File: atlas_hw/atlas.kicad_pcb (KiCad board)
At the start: 4 copper layers, 71 x 73.4 mm, 192 parts, among them J1 USB_C_Receptacle_USB2.0, J10 PSP_LCD, J2 DEBUG_STM, J3 PSP_TOUCH, J4 DEBUG_NRF, J5 CELL_THERM, J8 Micro_SD_Card_Det, J9 PSP_LCD_BL, Q1 Q_NMOS_DGS, Q2 Q_NMOS_DGS, Q3 Q_NMOS_DGS, Q4 Q_NMOS_DGS, Q5 Q_NMOS_DGS, SW1 SReset, SW2 Power, SW3 ResetSTM, SW4 ResetNRF, U1 STM32H723VITx, U10 BQ25611D, U11 STM6601CA2BDM6F, U12 BGU7007, U13 LSF0108, U14 NPP600SNADJ, U15 TPS61073, U16 PAM2841, U2 W957A8MFYA5I, U3 MCP1811B, U4 TLV62569DBV, U5 nRF52810-QCxx, U6 LC709203F, U7 Teseo-LIV3F, U8 MS5637, U9 MC6470, Y1 16M, Y2 32k, Y3 32M, Y4 32k

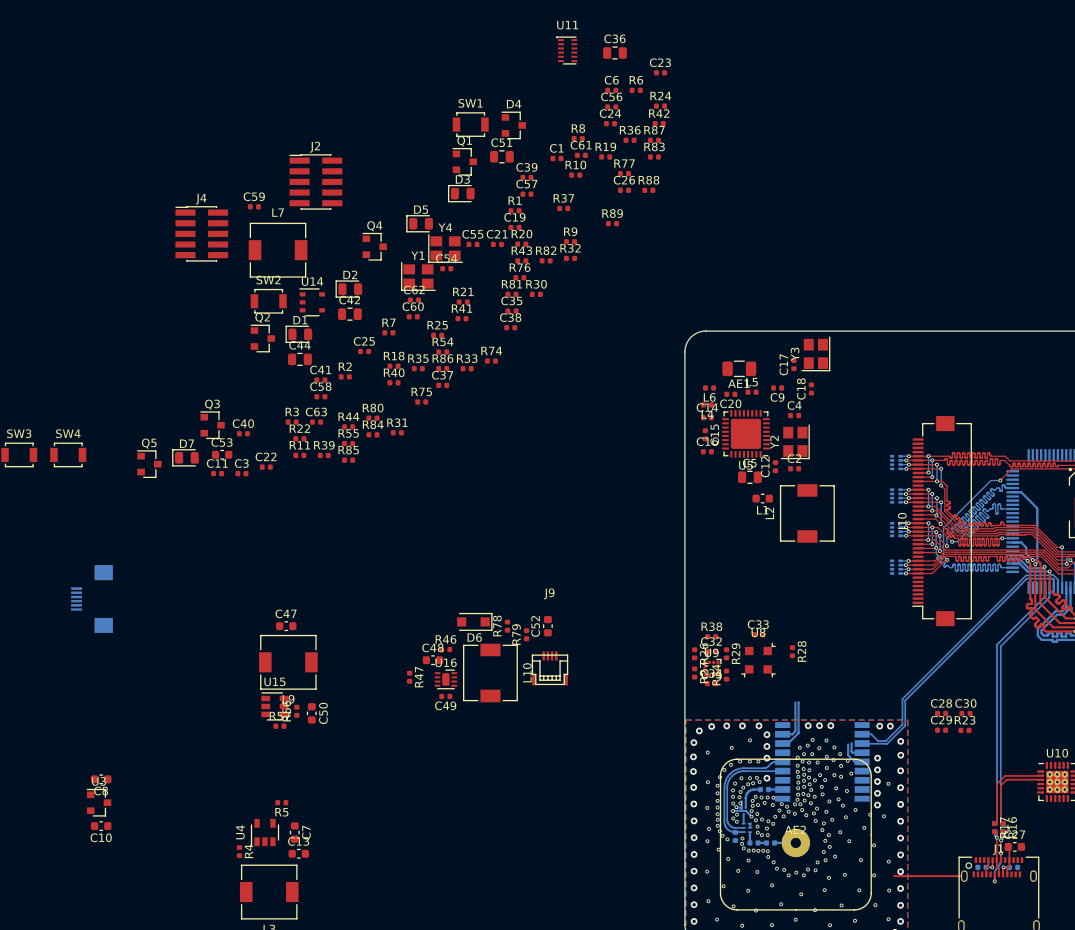
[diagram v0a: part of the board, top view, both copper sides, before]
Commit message: added attiny402 as sps
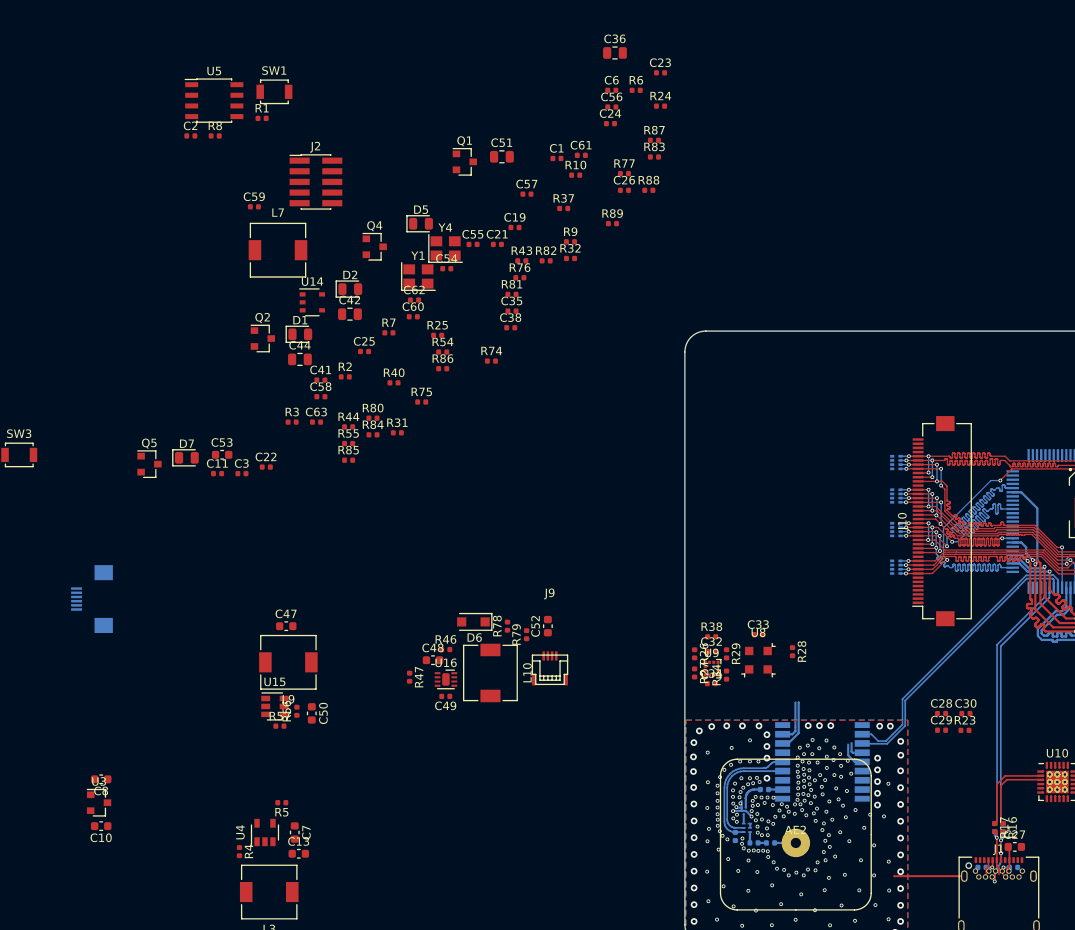
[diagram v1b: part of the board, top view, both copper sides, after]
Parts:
- removed AE1: CHIP, Resistor_SMD:R_1206_3216Metric
- removed C12: 100p, Capacitor_SMD:C_0402_1005Metric
- removed C14, C17, C18: 1p, Capacitor_SMD:C_0402_1005Metric
- removed C15: NP, Capacitor_SMD:C_0402_1005Metric
- removed C16, C39, C9: 0.1u, Capacitor_SMD:C_0402_1005Metric
- removed C20: 2.2p, Capacitor_SMD:C_0402_1005Metric
- removed C37, C40: 10u, Capacitor_SMD:C_0402_1005Metric
- removed C4: 12p, Capacitor_SMD:C_0402_1005Metric
- removed C5: 10u, Capacitor_SMD:C_0805_2012Metric
- removed D3: NRF_STATUS, LED_SMD:LED_0805_2012Metric
- removed D4: DC, Package_TO_SOT_SMD:SOT-23
- removed J4: DEBUG_NRF, Connector_PinHeader_1.27mm:PinHeader_2x05_P1.27mm_Vertical_SMD
- removed L1: 3.9n, Inductor_SMD:L_0603_1608Metric
- removed L2: 15u, Inductor_SMD:L_6.3x6.3_H3
- removed L4, L6: 3.9n, Inductor_SMD:L_0402_1005Metric
- removed L5: NP, Inductor_SMD:L_0402_1005Metric
- removed Q3: Q_NMOS_DGS, Package_TO_SOT_SMD:SOT-23
- removed R11, R35: 1k, Resistor_SMD:R_0402_1005Metric
- removed R18, R20, R21, R22, R41, R42: NP, Resistor_SMD:R_0402_1005Metric
- removed R19: 0, Resistor_SMD:R_0402_1005Metric
- removed R30: 10k, Resistor_SMD:R_0402_1005Metric
- removed R33, R36, R39: 100k, Resistor_SMD:R_0402_1005Metric
- removed SW2: Power, Button_Switch_SMD:SW_SPST_B3U-1000P
- removed SW4: ResetNRF, Button_Switch_SMD:SW_SPST_B3U-1000P
- removed U11: STM6601CA2BDM6F, Package_DFN_QFN:TDFN-12_2x3mm_P0.5mm
- removed Y2: 32k, Crystal:Crystal_SMD_3225-4Pin_3.2x2.5mm
- removed Y3: 32M, Crystal:Crystal_SMD_3225-4Pin_3.2x2.5mm
- C2: value 12p -> 0.1u
- J1: footprint Connector_USB:USB_C_Receptacle_Amphenol_12401610E4-2A -> Connector_USB:USB_C_Receptacle_Amphenol_12401548E4-2A
- R1: value 0 -> 100k
- SW1: value SReset -> ON_OFF
- U5: value nRF52810-QCxx -> ATtiny402-SS; footprint Package_DFN_QFN:QFN-32-1EP_5x5mm_P0.5mm_EP3.6x3.6mm -> Package_SO:SOIC-8_3.9x4.9mm_P1.27mm
- moved C2 82.3 mm to (134.4, 83.7)
- moved U5 74.9 mm to (137.2, 79.5), turned to 0 degrees
- moved R8 43.4 mm to (137.3, 83.7)
- moved R1 32.2 mm to (142.9, 81.6)
- moved SW1 23.8 mm to (144.4, 78.4)
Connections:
- net /BTN_DOWN renamed Net-(U1-Pad17)
- net /BTN_ENTER renamed Net-(U1-Pad16)
- net /BTN_LEFT renamed Net-(U1-Pad18)
- net /BTN_RIGHT renamed Net-(U1-Pad25)
- net /BTN_UP renamed Net-(U1-Pad24)
- net /EN_SD_PWR renamed Net-(U1-Pad85)
- net Net-(U5-Pad6) renamed /PWR_CTRL_UPDI
- C2 pad 2: /XL1_NRF -> /VCC_BACKUP
- C6 pad 1: Net-(C6-Pad1) -> /VCC_BACKUP
- R1 pad 1: Net-(C6-Pad1) -> /PWR_EN_O
- R8 pad 1: /NRF_STATUS -> /PWR_SW_I
- R8 pad 2: GND -> /VCC_BACKUP
- SW1 pad 2: Net-(R18-Pad1) -> /PWR_SW_I
- U1 pad 1: /SP4_SCK_NRF -> Net-(U1-Pad1)
- U1 pad 2: /NRF_INT -> Net-(U1-Pad2)
- U1 pad 4: /SP4_MISO_NRF -> Net-(U1-Pad4)
- U1 pad 5: /SP4_MOSI_NRF -> Net-(U1-Pad5)
- U1 pad 6: Net-(C6-Pad1) -> /VCC_BACKUP
- U1 pad 86: /PWR_MCU_HOLD -> /PWR_ACK_I
- U1 pad 87: /PWR_BTN_OUT -> /PWR_SW_O
- U1 pad 88: /PWR_MCU_INT -> Net-(U1-Pad88)
- U1 pad 97: /UART8_RX_NRF -> Net-(U1-Pad97)
- U1 pad 98: /UART8_TX_NRF -> Net-(U1-Pad98)
- U4 pad 1: /EN_MCU_PWR -> /PWR_EN_O
- U5 pad 1: /DEC1 -> /VCC_BACKUP
- U5 pad 2: /XL1_NRF -> /PWR_SW_I
- U5 pad 3: /XL2_NRF -> /PWR_EN_O
- U5 pad 4: Net-(U5-Pad4) -> /PWR_ACK_I
- U5 pad 5: Net-(U5-Pad5) -> /PWR_SW_O
- U5 pad 7: Net-(U5-Pad7) -> /DEBUG_NRESET_STM
- U5 pad 8: /NRF_INT -> GND
- U6 pad : GND -> (no net)
- U7 pad 10: GND -> Net-(C43-Pad2)
- U7 pad 11: Net-(C43-Pad2) -> (no net)
- U7 pad 18: Net-(U7-Pad18) -> (no net)

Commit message: rough blender model of casing further hw changes
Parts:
- removed AE2: 2088900001, atlas:2088900001
- removed C43, C46: 120p, Capacitor_SMD:C_0402_1005Metric
- removed C45: 0.1u, Capacitor_SMD:C_0402_1005Metric
- removed F1: B39162B8813P810, Filter:Filter_1109-5_1.1x0.9mm
- removed L8: 5n6, Inductor_SMD:L_0402_1005Metric
- removed U12: BGU7007, atlas:6-XSON_1.5x1.0mm_0.5mm
- removed U7: Teseo-LIV3F, RF_Module:ublox_MAX
- added REF**: BGM220P, atlas:BGM220P, F.Cu at (229.8, 83.3)
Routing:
- net /GPS_VCC_RF: track 15.7 -> 0.00 mm
- net /GPS_ANT_OFF: track 14.2 -> 0.00 mm
- net /LPUART1_RX_GPS: track 34.5 -> 24.8 mm
- net /LPUART1_TX_GPS: track 34.9 -> 25.9 mm
- net /I2C_SDA_SENSOR: track 6.08 -> 0.00 mm
- net /I2C_SCL_SENSOR: track 5.11 -> 0.00 mm
- net GND: track 13.2 -> 8.39 mm, vias 253 -> 0
- net Net-(C43-Pad1): track 3.54 -> 0.00 mm
- net /GPS_WAKEUP: track 3.29 -> 0.00 mm
- net Net-(AE2-Pad1): track 2.86 -> 0.00 mm
- net /GPS_1PPS: track 2.35 -> 0.00 mm
- net Net-(C43-Pad2): track 1.69 -> 0.00 mm
- net Net-(L8-Pad1): track 1.24 -> 0.00 mm
- net Net-(F1-Pad1): track 1.06 -> 0.00 mm
- net Net-(C46-Pad2): track 1.00 -> 0.00 mm
- removed copper zone on B.Cu, net GND
- removed copper zone on F.Cu, net GND
- removed copper zone on In1.Cu, net GND
- removed copper zone on In2.Cu, net GND

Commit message: begining hw layout
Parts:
- removed C28, C29, C30: 0.1u, Capacitor_SMD:C_0402_1005Metric
- removed Q2: Q_NMOS_DGS, Package_TO_SOT_SMD:SOT-23
- removed REF**: BGM220P, atlas:BGM220P
- added AE1: Antenna_Shield, Connector_Coaxial:U.FL_Hirose_U.FL-R-SMT-1_Vertical, F.Cu at (137.2, 100.3)
- added C4: 56p, Capacitor_SMD:C_0402_1005Metric, F.Cu at (170.4, 93.4)
- added C5: 0.1u, Capacitor_SMD:C_0603_1608Metric, F.Cu at (180.2, 71.3)
- added C9: 1u, Capacitor_SMD:C_0603_1608Metric, F.Cu at (136.7, 112.1)
- added D10: STM_STATUS_R, LED_SMD:LED_0805_2012Metric, F.Cu at (155.8, 91.2)
- added D3: GPS_3DF, LED_SMD:LED_0805_2012Metric, F.Cu at (162.0, 82.1)
- added D4: MCU_3V3, LED_SMD:LED_0805_2012Metric, F.Cu at (169.5, 77.4)
- added D8: STM_STATUS_L, LED_SMD:LED_0805_2012Metric, F.Cu at (176.0, 71.9)
- added D9: STM_STATUS_0, LED_SMD:LED_0805_2012Metric, F.Cu at (166.4, 82.1)
- added F1: SF14-1575F5UUC1, Filter:Filter_1411-5_1.4x1.1mm, F.Cu at (160.5, 71.4)
- added J4: DEBUG_NCP, Connector_PinHeader_1.27mm:PinHeader_2x05_P1.27mm_Vertical_SMD, B.Cu at (86.2, 54.3)
- added J6: LPM027M128B, Connector_FFC-FPC:Hirose_FH12-10S-0.5SH_1x10-1MP_P0.50mm_Horizontal, B.Cu at (61.2, 73.1)
- added J7: FLEX_12380-03, Connector_FFC-FPC:TE_84952-4_1x04-1MP_P1.0mm_Horizontal, F.Cu at (148.0, 65.5)
- added R11: 1k, Resistor_SMD:R_0402_1005Metric, F.Cu at (168.1, 87.1)
- added R18: 1k, Resistor_SMD:R_0402_1005Metric, F.Cu at (167.5, 97.0)
- added R19: 1k, Resistor_SMD:R_0402_1005Metric, F.Cu at (180.9, 83.1)
- added R20: 10k, Resistor_SMD:R_0402_1005Metric, F.Cu at (176.9, 87.1)
- added R21: 0, Resistor_SMD:R_0402_1005Metric, F.Cu at (119.3, 78.7)
- added R22: 0, Resistor_SMD:R_0402_1005Metric, F.Cu at (160.4, 104.4)
- added R30: 0, Resistor_SMD:R_0402_1005Metric, F.Cu at (154.5, 106.5)
- added R33: 4.7k, Resistor_SMD:R_0402_1005Metric, F.Cu at (148.7, 108.3)
- added R35: 4.7k, Resistor_SMD:R_0402_1005Metric, F.Cu at (147.9, 110.3)
- added R36: 100k, Resistor_SMD:R_0402_1005Metric, F.Cu at (180.8, 77.2)
- added R39: 0, Resistor_SMD:R_0402_1005Metric, F.Cu at (151.6, 104.5)
- added R41: 100k, Resistor_SMD:R_0402_1005Metric, F.Cu at (161.7, 95.7)
- added R42: 100k, Resistor_SMD:R_0402_1005Metric, F.Cu at (174.0, 87.5)
- added R45: 100, Resistor_SMD:R_0402_1005Metric, F.Cu at (161.7, 97.7)
- added R48: 100, Resistor_SMD:R_0402_1005Metric, F.Cu at (155.8, 96.5)
- added R49: 100, Resistor_SMD:R_0402_1005Metric, F.Cu at (145.0, 110.5)
- added U11: L96-M33, atlas:L96, F.Cu at (105.8, 97.9)
- added U12: BGU7007, atlas:6-XSON_1.5x1.0mm_0.5mm, F.Cu at (115.8, 94.3)
- added U7: BGM220P, atlas:BGM220P, B.Cu at (98.0, 66.4)
- D2: value STM_STATUS -> STM_STATUS_B
- J2: moved to B.Cu
- J3, J5, R12, R13, R14, R15, RN1, RN2, RN3, RN4, RN5, RN6, U1: moved to F.Cu
- J8: footprint Connector_Card:microSD_HC_Hirose_DM3D-SF -> Connector_Card:microSD_HC_Hirose_DM3AT-SF-PEJM5; moved to B.Cu
- L10, L3, L7, L9: footprint Inductor_SMD:L_6.3x6.3_H3 -> Inductor_SMD:L_Bourns-SRN4018
- R1, R6: value 100k -> 10k
- R23: value 100k -> 0
- R28, R29: value NP -> 4.7k
- R7, R8: value 100k -> 1k
- SW1: value ON_OFF -> ResetNCP
- U2: value W957A8MFYA5I -> S27KL0641DABHV023; moved to B.Cu
- U5: value ATtiny402-SS -> MX25L3233FM2I-08G; footprint Package_SO:SOIC-8_3.9x4.9mm_P1.27mm -> Package_SO:SSOP-8_5.25x5.24mm_P1.27mm; moved to B.Cu
- moved J8 209.2 mm to (64.8, 57.8)
- moved U13 190.6 mm to (68.0, 65.1), turned to 90 degrees
- moved J1 182.2 mm to (60.8, 109.8), turned to 270 degrees
- moved U1 180.0 mm to (67.9, 78.4), turned to 0 degrees
- moved U2 179.8 mm to (66.3, 91.3), turned to 270 degrees
- moved J10 149.9 mm to (82.8, 76.8)
- moved U6 125.9 mm to (175.5, 64.5), turned to 0 degrees
- moved C31 115.9 mm to (165.8, 84.8), turned to 0 degrees
- moved J5 115.7 mm to (157.8, 76.8)
- moved U10 114.7 mm to (151.7, 85.2)
- moved RN4 113.2 mm to (124.5, 72.5), turned to 0 degrees
- moved L3 111.2 mm to (168.9, 65.7), turned to 0 degrees
- moved RN3 110.1 mm to (115.8, 91.3), turned to 0 degrees
- moved R15 108.8 mm to (187.7, 66.3), turned to 0 degrees
- moved R13 107.7 mm to (174.3, 80.5)
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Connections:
- net Net-(U1-Pad25) renamed /SW_R
- C2 pad 2: /VCC_BACKUP -> /VCC_MCU_3V3
- D1 pad 2: /VCC_MCU_3V3 -> /GPS_1PPS
- D2 pad 2: /VCC_MCU_3V3 -> /STM_STATUS_B
- J2 pad 6: Net-(J2-Pad6) -> /DEBUG_SWO_STM
- J3 pad 2: /I2C1_SCL_SYSTEM -> /I2C1_SDA_SYSTEM
- Q1 pad 2: /GPS_1PPS -> /T3C1_LCD_BL
- R1 pad 1: /PWR_EN_O -> /VCC_BACKUP
- R1 pad 2: /VCC_BACKUP -> /PWR_EN_O
- R10 pad 2: Net-(Q2-Pad1) -> GND
- R23 pad 1: GND -> Net-(R23-Pad1)
- R23 pad 2: /GPS_RESET -> /I2C_SCL_SENSOR
- R47 pad 2: /TIM4_CH3_LCD_BL_PWM -> /T3C1_LCD_BL
- R6 pad 1: /GPS_1PPS -> /PWR_ACK_I
- R7 pad 1: /STM_STATUS -> Net-(D3-Pad1)
- R8 pad 1: /PWR_SW_I -> Net-(D4-Pad1)
- R8 pad 2: /VCC_BACKUP -> GND
- R86 pad 1: /VCC_MCU_3V3 -> /VCC_BACKUP
- R9 pad 2: Net-(Q1-Pad1) -> GND
- SW1 pad 1: GND -> /DEBUG_NRESET_NCP
- SW1 pad 2: /PWR_SW_I -> GND
- U1 pad 1: Net-(U1-Pad1) -> /SPI4_SCK_APP
- U1 pad 16: Net-(U1-Pad16) -> /STM_STATUS_L
- U1 pad 17: Net-(U1-Pad17) -> /STM_STATUS_0
- U1 pad 18: Net-(U1-Pad18) -> /STM_STATUS_R
- U1 pad 2: Net-(U1-Pad2) -> /SPI4_OPT_LCD_NCS
- U1 pad 22: /STC911_INT -> /SW_C
- U1 pad 23: /LC709203_INT -> /SW_L
- U1 pad 24: Net-(U1-Pad24) -> /~USB_DET
- U1 pad 3: /~USB_DET -> /SPI4_FLASH_NCS
- U1 pad 32: Net-(U1-Pad32) -> /EN_LCD_PWR
- U1 pad 4: Net-(U1-Pad4) -> /SPI4_MISO_APP
- U1 pad 41: /OCTOSPIM_P1_NPS -> /OCTOSPIM_P1_NCS
- U1 pad 5: Net-(U1-Pad5) -> /SPI4_MOSI_APP
- U1 pad 51: /OCTOSPIM_P1_NPLK -> /PWR_ACK_NCP
- U1 pad 52: Net-(U1-Pad52) -> /USART3_CTS_NCP
- U1 pad 53: Net-(U1-Pad53) -> /USART3_RTS_NCP
- U1 pad 54: Net-(U1-Pad54) -> /PWR_SW_NCP
- U1 pad 55: /MC6470_INTA -> /USART3_TX_NCP
- U1 pad 56: /MC6470_INTM -> /USART3_RX_NCP
- U1 pad 57: /LTDC_G3 -> /MC6470_INTA
- U1 pad 58: /STM_STATUS -> /MC6470_INTM
- U1 pad 59: /I2C_SCL_SENSOR -> /I2C4_SCL_SYSTEM
- U1 pad 60: /I2C_SDA_SENSOR -> /I2C4_SDA_SYSTEM
- U1 pad 61: /TIM4_CH3_LCD_BL_PWM -> /GPS_FORCE_ON
- U1 pad 62: /EN_LCD_PWR -> /GPS_EXTINT
- U1 pad 7: /BQ25611_INT -> /STC911_INT
- U1 pad 85: Net-(U1-Pad85) -> /LC709203_INT
- U1 pad 86: /PWR_ACK_I -> Net-(U1-Pad86)
- U1 pad 87: /PWR_SW_O -> Net-(U1-Pad87)
- U1 pad 89: /GPS_RESET -> /DEBUG_SWO_STM
- U1 pad 90: /GPS_WAKEUP -> /T3C1_LCD_BL
- U1 pad 93: /I2C1_SCL_SYSTEM -> /I2C1_SDA_SYSTEM
- U1 pad 97: Net-(U1-Pad97) -> /BQ25611_INT
- U1 pad 98: Net-(U1-Pad98) -> /OPT_LCD_COM_INV
- U10 pad 6: /I2C1_SCL_SYSTEM -> /I2C1_SDA_SYSTEM
- U16 pad 3: /TIM4_CH3_LCD_BL_PWM -> /T3C1_LCD_BL
- U2 pad A4: /MCU_LV_RESET -> /DEBUG_NRESET_STM
- U2 pad B1: /OCTOSPIM_P1_NPLK -> Net-(U2-PadB1)
- U5 pad 1: /VCC_BACKUP -> /SPI4_FLASH_CS
- U5 pad 2: /PWR_SW_I -> /SPI4_MISO_APP
- U5 pad 3: /PWR_EN_O -> Net-(U5-Pad3)
- U5 pad 4: /PWR_ACK_I -> GND
- U5 pad 5: /PWR_SW_O -> /SPI4_MOSI_APP
- U5 pad 6: /PWR_CTRL_UPDI -> /SPI4_SCK_APP
- U5 pad 7: /DEBUG_NRESET_STM -> Net-(U5-Pad7)
- U5 pad 8: GND -> /VCC_MCU_3V3
- U6 pad 7: /I2C1_SCL_SYSTEM -> /I2C1_SDA_SYSTEM
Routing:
- net /LTDC_R5: track 43.7 -> 0.00 mm, vias 4 -> 0
- net /LTDC_R4: track 41.6 -> 0.00 mm, vias 4 -> 0
- net /LTDC_R6: track 39.4 -> 0.00 mm, vias 4 -> 0
- net /LTDC_B7: track 38.7 -> 0.00 mm, vias 4 -> 0
- net /LTDC_VS: track 37.8 -> 0.00 mm, vias 4 -> 0
- net /LTDC_G7: track 37.1 -> 0.00 mm, vias 4 -> 0
- net /LTDC_R7: track 36.2 -> 0.00 mm, vias 4 -> 0
- net /LTDC_HS: track 36.2 -> 0.00 mm, vias 2 -> 0
- net /LTDC_B5: track 35.6 -> 0.00 mm, vias 4 -> 0
- net /LTDC_G5: track 35.6 -> 0.00 mm, vias 4 -> 0
- net /LTDC_B4: track 35.3 -> 0.00 mm, vias 4 -> 0
- net /LTDC_G4: track 35.1 -> 0.00 mm, vias 4 -> 0
- net /LTDC_B6: track 33.5 -> 0.00 mm, vias 3 -> 0
- net /LTDC_DE: track 32.4 -> 0.00 mm, vias 2 -> 0
- net /LTDC_CK: track 31.5 -> 0.00 mm, vias 2 -> 0
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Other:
- board size 71 x 73.4 mm -> 50 x 70 mm

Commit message: layout of sd, octo, place sensors, connectors
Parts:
- removed RN5, RN6: R_Pack04, Resistor_SMD:R_Array_Concave_4x0402
- AE1, C23, C24, J5, U1, U13, U8: moved to B.Cu
- J2, J4, J6, U2: moved to F.Cu
- J8: footprint Connector_Card:microSD_HC_Hirose_DM3AT-SF-PEJM5 -> Connector_Card:microSD_HC_Hirose_DM3BT-DSF-PEJS
- SW1, SW3: footprint Button_Switch_SMD:SW_SPST_B3U-1000P -> Jumper:SolderJumper-2_P1.3mm_Open_Pad1.0x1.5mm
- moved R55 192.5 mm to (45.8, 256.5)
- moved C1 192.5 mm to (70.9, 243.1)
- moved C19 192.5 mm to (47.5, 266.4)
- moved C2 192.5 mm to (66.9, 247.1)
- moved C21 192.5 mm to (35.8, 266.3)
- moved C27 192.5 mm to (50.0, 251.5)
- moved C3 192.5 mm to (60.4, 253.4)
- moved C38 192.5 mm to (54.6, 253.1)
- moved C4 192.5 mm to (60.4, 251.4)
- moved C47 192.5 mm to (42.0, 258.2)
- moved C49 192.5 mm to (46.6, 268.4)
- moved C5 192.5 mm to (70.2, 229.3)
- moved C50 192.5 mm to (70.2, 224.3)
- moved C51 192.5 mm to (37.8, 261.9)
- moved C52 192.5 mm to (65.8, 232.7)
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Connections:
- J3 pad 1: /I2C1_SCL_SYSTEM -> /I2C1_SCL_SENSOR
- J3 pad 2: /I2C1_SDA_SYSTEM -> /I2C1_SDA_SENSOR
- R23 pad 2: /I2C_SCL_SENSOR -> /I2C4_SCL_SYSTEM
- R28 pad 2: /I2C_SCL_SENSOR -> /I2C1_SCL_SENSOR
- R29 pad 2: /I2C_SDA_SENSOR -> /I2C1_SDA_SENSOR
- R30 pad 2: /I2C_SDA_SENSOR -> /I2C4_SDA_SYSTEM
- R33 pad 2: /I2C1_SDA_SYSTEM -> /I2C4_SDA_SYSTEM
- R35 pad 2: /I2C1_SDA_SYSTEM -> /I2C4_SDA_SYSTEM
- RN1 pad 1: /LTDC_R4 -> /LTDC_R7
- RN1 pad 2: /LTDC_R5 -> /LTDC_R6
- RN1 pad 3: /LTDC_R6 -> /LTDC_R5
- RN1 pad 4: /LTDC_R7 -> /LTDC_R4
- RN2 pad 1: /LTDC_G4 -> /LTDC_G7
- RN2 pad 2: /LTDC_G5 -> /LTDC_G6
- RN2 pad 3: /LTDC_G6 -> /LTDC_G5
- RN2 pad 4: /LTDC_G7 -> /LTDC_G4
- RN3 pad 1: /LTDC_B4 -> /LTDC_B7
- RN3 pad 2: /LTDC_B5 -> /LTDC_B6
- RN3 pad 3: /LTDC_B6 -> /LTDC_B5
- RN3 pad 4: /LTDC_B7 -> /LTDC_B4
- RN4 pad 1: /LTDC_CK -> /LTDC_VS
- RN4 pad 2: /LTDC_DE -> /LTDC_HS
- RN4 pad 3: /LTDC_HS -> /LTDC_DE
- RN4 pad 4: /LTDC_VS -> /LTDC_CK
- U1 pad 92: /I2C1_SCL_SYSTEM -> /I2C1_SCL_SENSOR
- U1 pad 93: /I2C1_SDA_SYSTEM -> /I2C1_SDA_SENSOR
- U10 pad 5: /I2C1_SCL_SYSTEM -> /I2C4_SCL_SYSTEM
- U10 pad 6: /I2C1_SDA_SYSTEM -> /I2C4_SDA_SYSTEM
- U11 pad 29: Net-(U11-Pad29) -> /GPS_FORCE_ON
- U11 pad 7: Net-(U11-Pad7) -> /GPS_EXTINT
- U13 pad 10: /SDMMC1_D1 -> Net-(R88-Pad1)
- U13 pad 11: /SD_D1 -> Net-(R89-Pad1)
- U13 pad 12: /SD_D0 -> /SD_D1
- U13 pad 13: /SD_CLK -> /SD_D0
- U13 pad 14: /SD_CLK -> /SD_D2
- U13 pad 15: /SD_CMD -> /SD_D3
- U13 pad 16: /SD_D3 -> /SD_CLK
- U13 pad 17: /SD_D2 -> /SD_CLK
- U13 pad 18: Net-(R89-Pad1) -> /SD_CMD
- U13 pad 3: Net-(R88-Pad1) -> /SDMMC1_CMD
- U13 pad 4: /SDMMC1_D2 -> /SDMMC1_CK
- U13 pad 5: /SDMMC1_D3 -> /SDMMC1_CKIN
- U13 pad 6: /SDMMC1_CMD -> /SDMMC1_D3
- U13 pad 7: /SDMMC1_CKIN -> /SDMMC1_D2
- U13 pad 8: /SDMMC1_CK -> /SDMMC1_D0
- U13 pad 9: /SDMMC1_D0 -> /SDMMC1_D1
- U2 pad A3: /OCTOSPIM_P1_NPS -> /OCTOSPIM_P1_NCS
- U6 pad 7: /I2C1_SDA_SYSTEM -> /I2C4_SDA_SYSTEM
- U6 pad 8: /I2C1_SCL_SYSTEM -> /I2C4_SCL_SYSTEM
- U8 pad 2: /I2C_SDA_SENSOR -> /I2C1_SDA_SENSOR
- U8 pad 3: /I2C_SCL_SENSOR -> /I2C1_SCL_SENSOR
- U9 pad 12: /I2C_SCL_SENSOR -> /I2C1_SCL_SENSOR
- U9 pad 2: /I2C_SDA_SENSOR -> /I2C1_SDA_SENSOR
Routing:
- net /LTDC_R4: track 0.00 -> 35.4 mm, vias 0 -> 1
- net /LTDC_VS: track 0.00 -> 30.5 mm, vias 0 -> 1
- net /LTDC_G4: track 0.00 -> 30.5 mm, vias 0 -> 3
- net /LTDC_R5: track 0.00 -> 30.4 mm, vias 0 -> 1
- net /LTDC_G5: track 0.00 -> 29.8 mm, vias 0 -> 3
- net /LTDC_R7: track 0.00 -> 29.5 mm, vias 0 -> 3
- net /LTDC_B4: track 0.00 -> 28.4 mm, vias 0 -> 3
- net /LTDC_B7: track 0.00 -> 27.2 mm, vias 0 -> 3
- net /LTDC_R6: track 0.00 -> 24.4 mm, vias 0 -> 3
- net /LTDC_DE: track 0.00 -> 23.4 mm, vias 0 -> 1
- net /LTDC_CK: track 0.00 -> 23.1 mm, vias 0 -> 1
- net /LTDC_G6: track 0.00 -> 22.8 mm, vias 0 -> 3
- net /LTDC_B5: track 0.00 -> 22.3 mm, vias 0 -> 3
- net /LTDC_G7: track 0.00 -> 17.5 mm, vias 0 -> 3
- net /SD_D1: track 0.00 -> 16.9 mm
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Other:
- board size 50 x 70 mm -> 67 x 70 mm
